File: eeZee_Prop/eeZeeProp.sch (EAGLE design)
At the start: 28 parts, among them Q1 5MHz, SW1 RESET, U1 P8X32A-Q44, U2 24LC256-I/ST, U3 NCP1117 3V3

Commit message: Rev 0.2 as built
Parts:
- U3: PARTNO SPX1117M3-L-3-3 -> NCP1117ST33T3G
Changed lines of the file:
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@@
 <?xml version="1.0" encoding="utf-8"?>
 <!DOCTYPE eagle SYSTEM "eagle.dtd">
-<eagle version="6.1">
+<eagle version="6.3">
 <drawing>
 <settings>
@@
 <grid distance="0.1" unitdist="inch" unit="inch" style="lines" multiple="1" display="no" altdistance="0.01" altunitdist="inch" altunit="inch"/>
 <layers>
-<layer number="1" name="Top" color="4" fill="1" visible="yes" active="no"/>
-<layer number="16" name="Bottom" color="1" fill="1" visible="yes" active="no"/>
-<layer number="17" name="Pads" color="2" fill="1" visible="yes" active="no"/>
-<layer number="18" name="Vias" color="2" fill="1" visible="yes" active="no"/>
-<layer number="19" name="Unrouted" color="6" fill="1" visible="yes" active="no"/>
-<layer number="20" name="Dimension" color="15" fill="1" visible="yes" active="no"/>
-<layer number="21" name="tPlace" color="7" fill="1" visible="yes" active="no"/>
-<layer number="22" name="bPlace" color="7" fill="1" visible="yes" active="no"/>
-<layer number="23" name="tOrigins" color="15" fill="1" visible="yes" active="no"/>
-<layer number="24" name="bOrigins" color="15" fill="1" visible="yes" active="no"/>
-<layer number="25" name="tNames" color="7" fill="1" visible="yes" active="no"/>
-<layer number="26" name="bNames" color="7" fill="1" visible="yes" active="no"/>
-<layer number="27" name="tValues" color="7" fill="1" visible="yes" active="no"/>
-<layer number="28" name="bValues" color="7" fill="1" visible="yes" active="no"/>
+<layer number="1" name="Top" color="4" fill="1" visible="no" active="no"/>
+<layer number="16" name="Bottom" color="1" fill="1" visible="no" active="no"/>
+<layer number="17" name="Pads" color="2" fill="1" visible="no" active="no"/>
+<layer number="18" name="Vias" color="2" fill="1" visible="no" active="no"/>
+<layer number="19" name="Unrouted" color="6" fill="1" visible="no" active="no"/>
+<layer number="20" name="Dimension" color="15" fill="1" visible="no" active="no"/>
+<layer number="21" name="tPlace" color="7" fill="1" visible="no" active="no"/>
+<layer number="22" name="bPlace" color="7" fill="1" visible="no" active="no"/>
+<layer number="23" name="tOrigins" color="15" fill="1" visible="no" active="no"/>
+<layer number="24" name="bOrigins" color="15" fill="1" visible="no" active="no"/>
+<layer number="25" name="tNames" color="7" fill="1" visible="no" active="no"/>
+<layer number="26" name="bNames" color="7" fill="1" visible="no" active="no"/>
+<layer number="27" name="tValues" color="7" fill="1" visible="no" active="no"/>
+<layer number="28" name="bValues" color="7" fill="1" visible="no" active="no"/>
 <layer number="29" name="tStop" color="7" fill="3" visible="no" active="no"/>
 <layer number="30" name="bStop" color="7" fill="6" visible="no" active="no"/>
@@
 <layer number="35" name="tGlue" color="7" fill="4" visible="no" active="no"/>
 <layer number="36" name="bGlue" color="7" fill="5" visible="no" active="no"/>
-<layer number="37" name="tTest" color="7" fill="1" visible="yes" active="no"/>
-<layer number="38" name="bTest" color="7" fill="1" visible="yes" active="no"/>
+<layer number="37" name="tTest" color="7" fill="1" visible="no" active="no"/>
+<layer number="38" name="bTest" color="7" fill="1" visible="no" active="no"/>
 <layer number="39" name="tKeepout" color="4" fill="11" visible="no" active="no"/>
 <layer number="40" name="bKeepout" color="1" fill="11" visible="no" active="no"/>
@@
 <layer number="44" name="Drills" color="7" fill="1" visible="no" active="no"/>
 <layer number="45" name="Holes" color="7" fill="1" visible="no" active="no"/>
-<layer number="46" name="Milling" color="3" fill="1" visible="yes" active="no"/>
-<layer number="47" name="Measures" color="7" fill="1" visible="yes" active="no"/>
-<layer number="48" name="Document" color="7" fill="1" visible="yes" active="no"/>
-<layer number="49" name="Reference" color="7" fill="1" visible="yes" active="no"/>
-<layer number="50" name="dxf" color="7" fill="1" visible="yes" active="no"/>
-<layer number="51" name="tDocu" color="7" fill="1" visible="yes" active="no"/>
-<layer number="52" name="bDocu" color="7" fill="1" visible="yes" active="no"/>
-<layer number="53" name="tGND_GNDA" color="7" fill="9" visible="yes" active="no"/>
-<layer number="54" name="bGND_GNDA" color="1" fill="9" visible="yes" active="no"/>
-<layer number="56" name="wert" color="7" fill="1" visible="yes" active="no"/>
+<layer number="46" name="Milling" color="3" fill="1" visible="no" active="no"/>
+<layer number="47" name="Measures" color="7" fill="1" visible="no" active="no"/>
+<layer number="48" name="Document" color="7" fill="1" visible="no" active="no"/>
+<layer number="49" name="Reference" color="7" fill="1" visible="no" active="no"/>
+<layer number="50" name="dxf" color="7" fill="1" visible="no" active="no"/>
+<layer number="51" name="tDocu" color="7" fill="1" visible="no" active="no"/>
+<layer number="52" name="bDocu" color="7" fill="1" visible="no" active="no"/>
+<layer number="53" name="tGND_GNDA" color="7" fill="9" visible="no" active="no"/>
+<layer number="54" name="bGND_GNDA" color="1" fill="9" visible="no" active="no"/>
+<layer number="56" name="wert" color="7" fill="1" visible="no" active="no"/>
 <layer number="91" name="Nets" color="2" fill="1" visible="yes" active="yes"/>
 <layer number="92" name="Busses" color="1" fill="1" visible="yes" active="yes"/>
@@
 <schematic xreflabel="%F%N/%S.%C%R" xrefpart="/%S.%C%R">
 <attributes>
-<attribute name="DATABASE" value="./../../eagle/PARTSDB.txt"/>
+<attribute name="DATABASE" value="./../../../eagle/PARTSDB.txt"/>
 </attributes>
 <variantdefs>
@@
 <part name="VIN" library="supply1" deviceset="V+" device=""/>
 <part name="U3" library="SparkFun" deviceset="V_REG_LM1117" device="SOT223" value="NCP1117 3V3">
-<attribute name="PARTNO" value="SPX1117M3-L-3-3"/>
+<attribute name="PARTNO" value="NCP1117ST33T3G"/>
 </part>
 <part name="C2" library="rcl" deviceset="C-US" device="C1206" value="10uF">

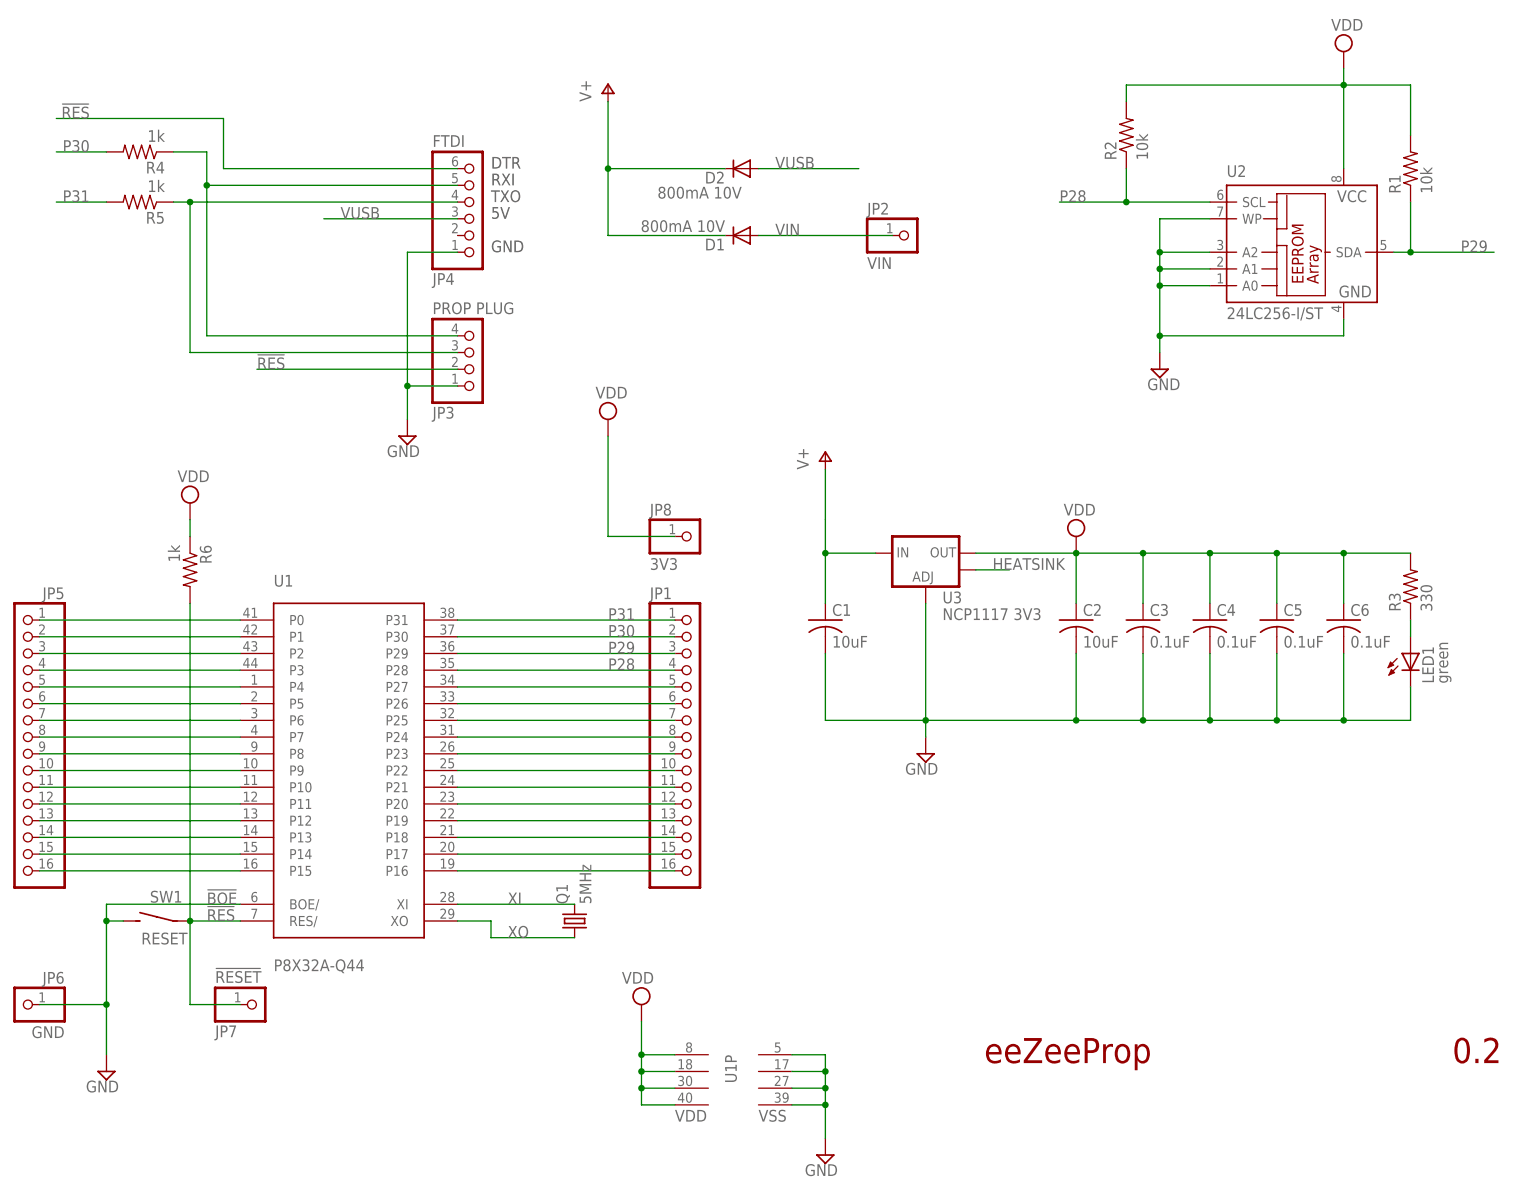
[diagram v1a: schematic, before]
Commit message: Revised reset circuit, added bypass for VIN diode, added BOE solder jumper
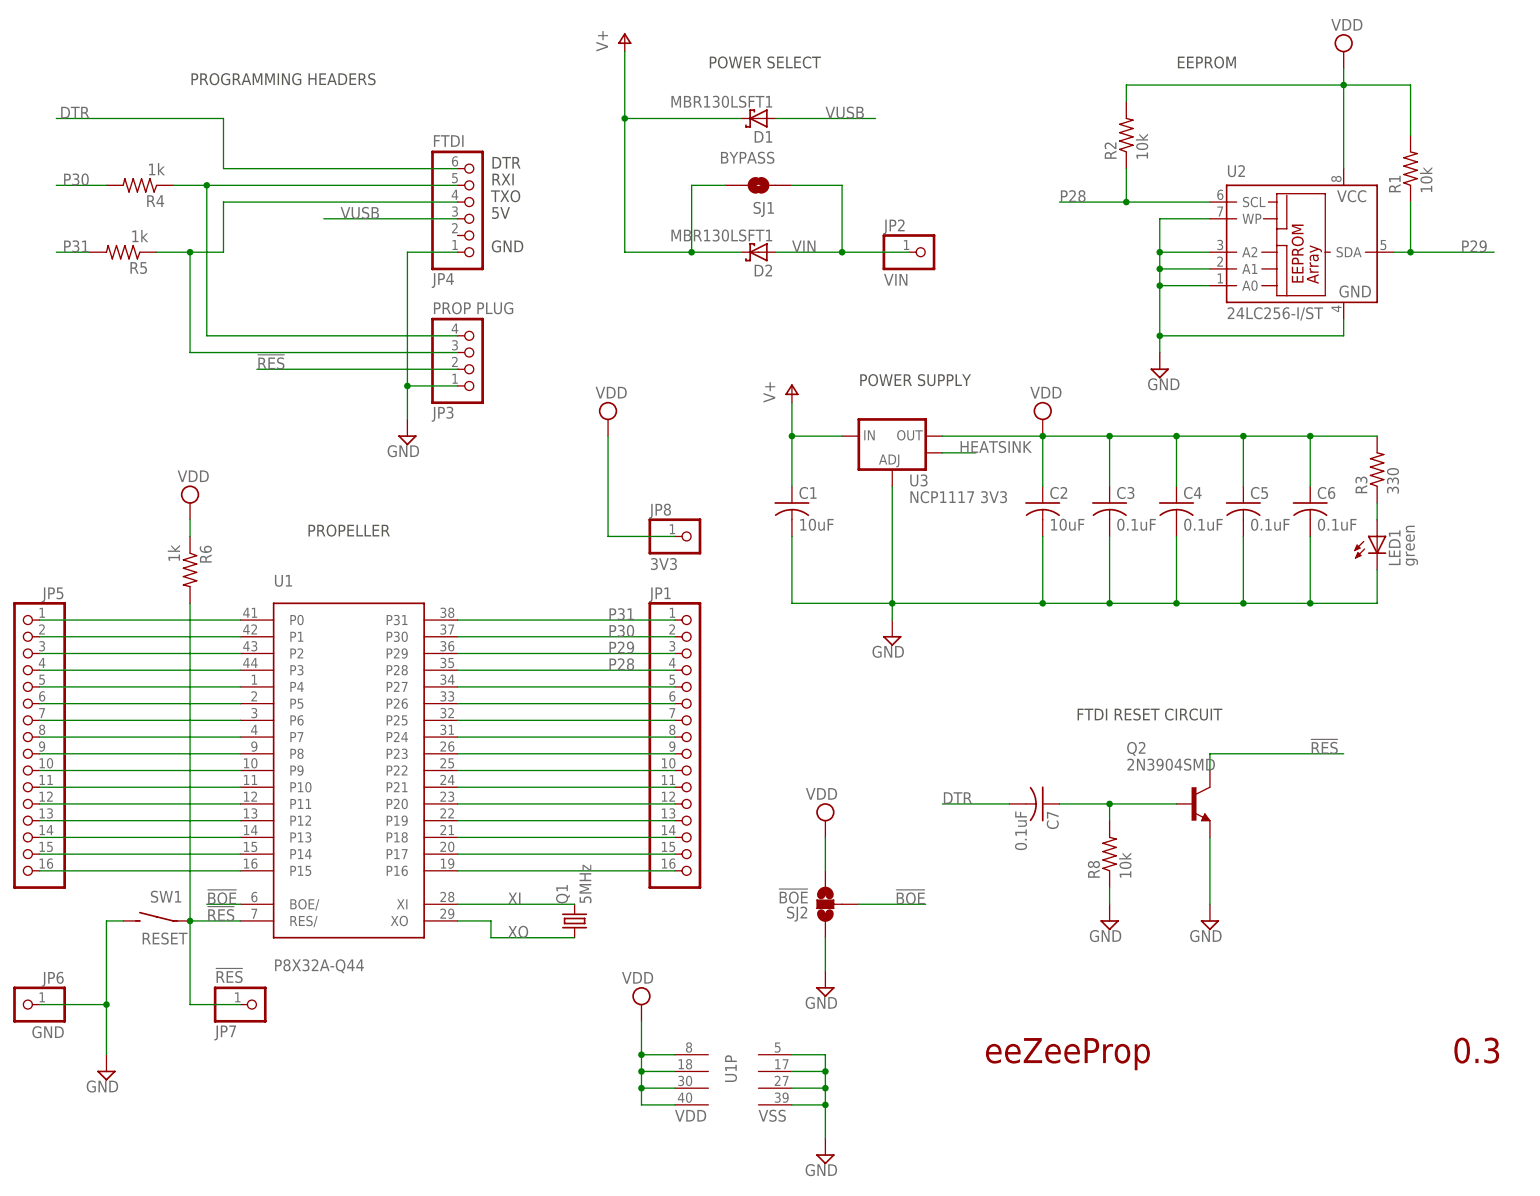
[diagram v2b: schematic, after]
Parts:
- added C7: 0.1uF, rcl:C-USC0603
- added Q2: 2N3904SMD, mes_transistors:2N3904SMD
- added R8: 10k, rcl:R-US_R0603
- added SJ1: BYPASS, SparkFun:SOLDERJUMPERNO
- added SJ2: !BOE, SparkFun:SOLDERJUMPER_2WAYS
- D1, D2: value 800mA 10V -> MBR130LSFT1; device diode:DIODE-SOD323-R -> mes_diode:SCHOTTKY-DIODE-MBR130LSFT1; PARTNO PMEG2015EA,115 -> MBR130LSFT1G
- JP3: device pinhead-2:PINHD-1X04_2.54-90°-S -> pinhead-2:PINHD-1X04_2.54-S
- JP7: value !RESET -> !RES
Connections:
- new net !BOE: SJ2.2, U1P8X32A-Q44.BOE/
- new net DTR: C7.2, JP4.6
- new net N$31: C7.1, Q2.B, R8.2
- net !RES: now also Q2.C; no longer JP4.6
- net GND: now also Q2.E, R8.1, SJ2.1; no longer U1P8X32A-Q44.BOE/
- net V+: now also SJ1.2
- net VDD: now also SJ2.3
- net VIN: now also D2.A, SJ1.1; no longer D1.A
- net VUSB: now also D1.A; no longer D2.A
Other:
- note added: "0.3"
- note added: "EEPROM"
- note added: "FTDI RESET CIRCUIT"
- note added: "POWER SELECT"
- note added: "POWER SUPPLY"
- note added: "PROGRAMMING HEADERS"
- note added: "PROPELLER"
- note removed: "0.2"
- moved on the sheet: C1, C2, C3, C4, C5, C6, JP2, LED1, R3, R4, R5, U3
